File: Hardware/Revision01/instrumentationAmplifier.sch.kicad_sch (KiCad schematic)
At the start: 10 parts, among them J11 Conn_01x04, U4 TLV9062IDSGR

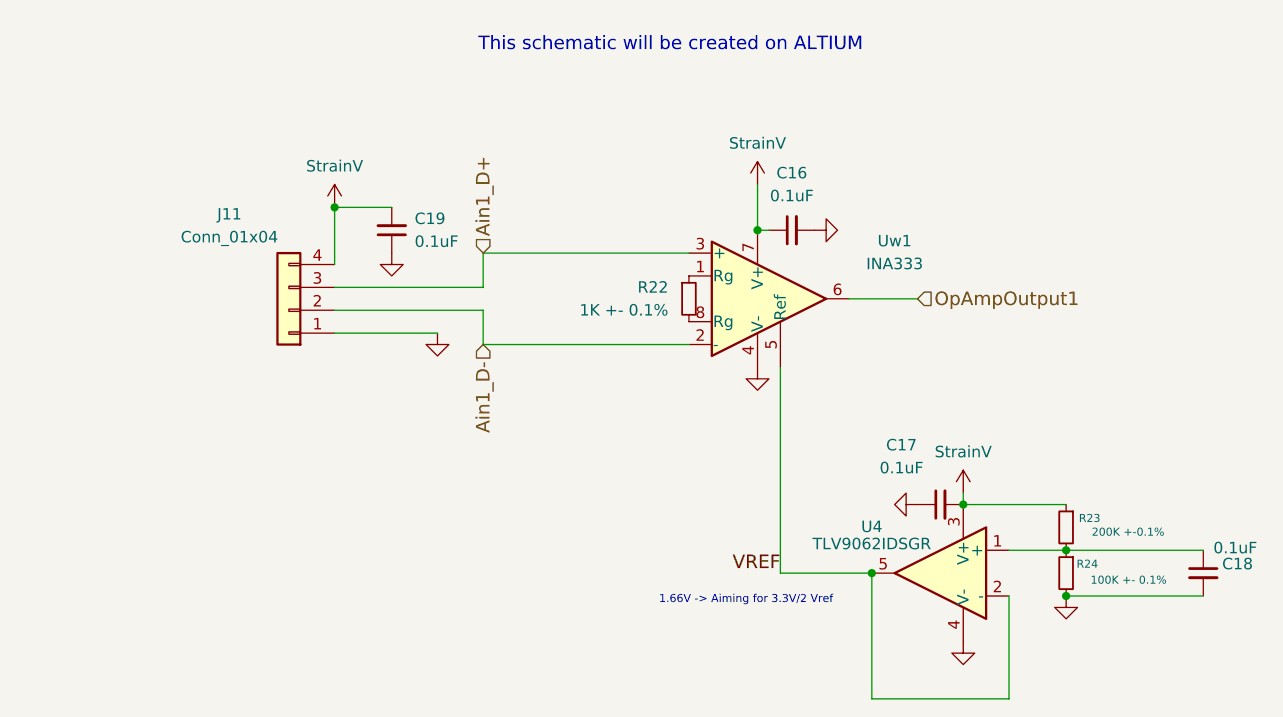
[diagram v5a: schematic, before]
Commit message: Small details on PART B, restarting component placement on PART A
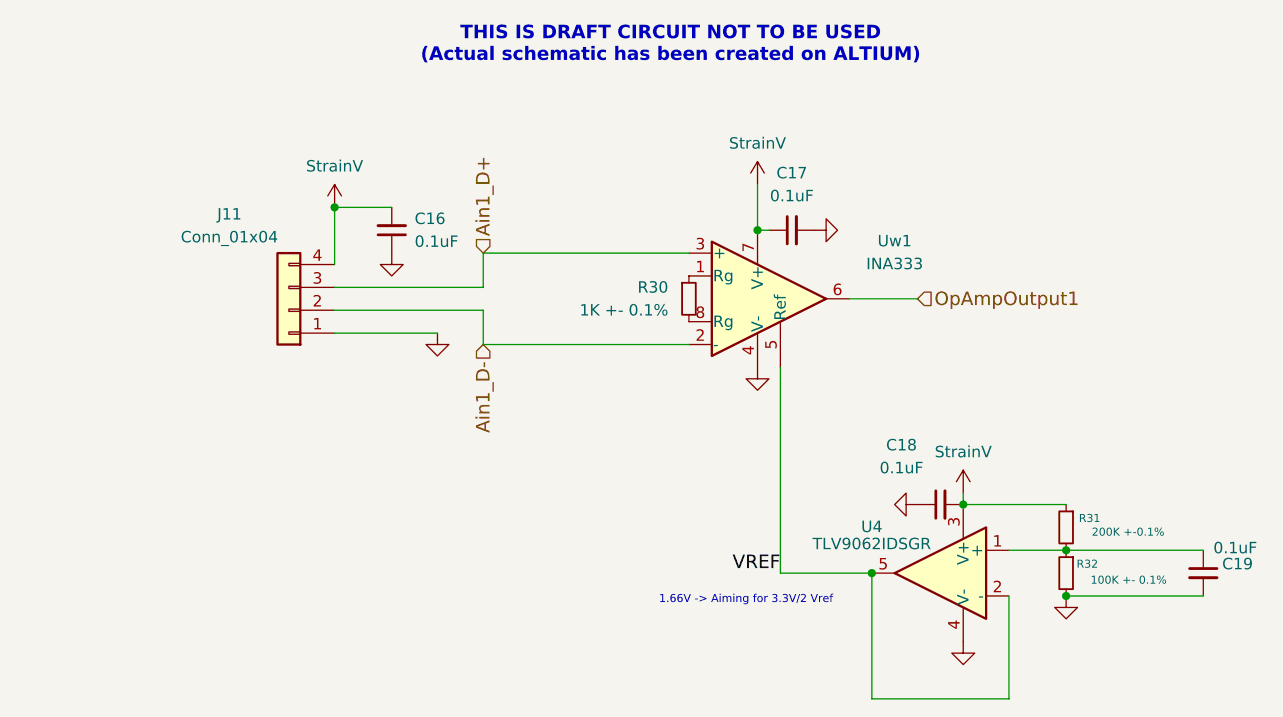
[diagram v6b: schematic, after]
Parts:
- renumbered C19 to C16, C16 to C17, C17 to C18, C18 to C19, R22 to R30, R23 to R31, R24 to R32
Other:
- note added: "THIS IS DRAFT CIRCUIT NOT TO BE USED (Actual schematic has been created on ALTIUM)"
- note removed: "This schematic will be created on ALTIUM"
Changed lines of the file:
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@@
 	(generator_version "9.0")
 	(paper "A4")
-	(text "This schematic will be created on ALTIUM"
+	(text "THIS IS DRAFT CIRCUIT NOT TO BE USED\n(Actual schematic has been created on ALTIUM)"
 		(exclude_from_sim no)
 		(at 127.508 56.896 0)
@@
 			(font
 				(size 1.4986 1.4986)
+				(thickness 0.2997)
+				(bold yes)
 			)
 		)
@@
 		(on_board no)
 		(dnp no)
-		(property "Reference" "#PWR060"
+		(property "Reference" "#PWR063"
 			(at 137.16 76.2 0)
 			(effects
@@
 			(project "Revision01"
 				(path "/955cc99e-a129-42cf-abc7-aa99813fdb5f/00000000-0000-0000-0000-00005eb1de63/14eb51a3-67a8-4f4f-b7c1-d030be0d073f"
-					(reference "#PWR060")
+					(reference "#PWR063")
 					(unit 1)
 				)
@@
 		(dnp no)
 		(fields_autoplaced yes)
-		(property "Reference" "C19"
+		(property "Reference" "C16"
 			(at 99.06 76.1935 0)
 			(effects
@@
 			(project "Revision01"
 				(path "/955cc99e-a129-42cf-abc7-aa99813fdb5f/00000000-0000-0000-0000-00005eb1de63/14eb51a3-67a8-4f4f-b7c1-d030be0d073f"
-					(reference "C19")
+					(reference "C16")
 					(unit 1)
 				)
@@
 		(on_board no)
 		(dnp no)
-		(property "Reference" "#PWR068"
+		(property "Reference" "#PWR060"
 			(at 90.17 78.74 0)
 			(effects
@@
 			(project "Revision01"
 				(path "/955cc99e-a129-42cf-abc7-aa99813fdb5f/00000000-0000-0000-0000-00005eb1de63/14eb51a3-67a8-4f4f-b7c1-d030be0d073f"
-					(reference "#PWR068")
+					(reference "#PWR060")
 					(unit 1)
 				)
@@
 		(on_board no)
 		(dnp no)
-		(property "Reference" "R24"
+		(property "Reference" "R32"
 			(at 175.006 114.554 0)
 			(effects
@@
 			(project "Revision01"
 				(path "/955cc99e-a129-42cf-abc7-aa99813fdb5f/00000000-0000-0000-0000-00005eb1de63/14eb51a3-67a8-4f4f-b7c1-d030be0d073f"
-					(reference "R24")
+					(reference "R32")
 					(unit 1)
 				)
@@
 		(on_board no)
 		(dnp no)
-		(property "Reference" "#PWR064"
+		(property "Reference" "#PWR067"
 			(at 160.02 110.49 0)
 			(effects
@@
 			(project "Revision01"
 				(path "/955cc99e-a129-42cf-abc7-aa99813fdb5f/00000000-0000-0000-0000-00005eb1de63/14eb51a3-67a8-4f4f-b7c1-d030be0d073f"
-					(reference "#PWR064")
+					(reference "#PWR067")
 					(unit 1)
 				)
@@
 		(on_board no)
 		(dnp no)
-		(property "Reference" "C18"
+		(property "Reference" "C19"
 			(at 190.5 114.554 0)
 			(effects
@@
 			(project "Revision01"
 				(path "/955cc99e-a129-42cf-abc7-aa99813fdb5f/00000000-0000-0000-0000-00005eb1de63/14eb51a3-67a8-4f4f-b7c1-d030be0d073f"
-					(reference "C18")
+					(reference "C19")
 					(unit 1)
 				)
@@
 		(dnp no)
 		(fields_autoplaced yes)
-		(property "Reference" "#PWR067"
+		(property "Reference" "#PWR062"
 			(at 101.6 95.25 0)
 			(effects
@@
 			(project "Revision01"
 				(path "/955cc99e-a129-42cf-abc7-aa99813fdb5f/00000000-0000-0000-0000-00005eb1de63/14eb51a3-67a8-4f4f-b7c1-d030be0d073f"
-					(reference "#PWR067")
+					(reference "#PWR062")
 					(unit 1)
 				)
@@
 		(dnp no)
 		(fields_autoplaced yes)
-		(property "Reference" "#PWR061"
+		(property "Reference" "#PWR064"
 			(at 137.16 99.06 0)
 			(effects
@@
 			(project "Revision01"
 				(path "/955cc99e-a129-42cf-abc7-aa99813fdb5f/00000000-0000-0000-0000-00005eb1de63/14eb51a3-67a8-4f4f-b7c1-d030be0d073f"
-					(reference "#PWR061")
+					(reference "#PWR064")
 					(unit 1)
 				)
@@
 		(dnp no)
 		(fields_autoplaced yes)
-		(property "Reference" "C16"
+		(property "Reference" "C17"
 			(at 140.9763 71.12 90)
 			(effects
@@
 			(project "Revision01"
 				(path "/955cc99e-a129-42cf-abc7-aa99813fdb5f/00000000-0000-0000-0000-00005eb1de63/14eb51a3-67a8-4f4f-b7c1-d030be0d073f"
-					(reference "C16")
+					(reference "C17")
 					(unit 1)
 				)
@@
 		(on_board no)
 		(dnp no)
-		(property "Reference" "C17"
+		(property "Reference" "C18"
 			(at 153.162 101.346 90)
 			(effects
@@
 			(project "Revision01"
 				(path "/955cc99e-a129-42cf-abc7-aa99813fdb5f/00000000-0000-0000-0000-00005eb1de63/14eb51a3-67a8-4f4f-b7c1-d030be0d073f"
-					(reference "C17")
+					(reference "C18")
 					(unit 1)
 				)
@@
 		(on_board no)
 		(dnp no)
-		(property "Reference" "R22"
+		(property "Reference" "R30"
 			(at 127.254 83.82 0)
 			(effects
@@
 			(project "Revision01"
 				(path "/955cc99e-a129-42cf-abc7-aa99813fdb5f/00000000-0000-0000-0000-00005eb1de63/14eb51a3-67a8-4f4f-b7c1-d030be0d073f"
-					(reference "R22")
+					(reference "R30")
 					(unit 1)
 				)
@@
 		(dnp no)
 		(fields_autoplaced yes)
-		(property "Reference" "#PWR065"
+		(property "Reference" "#PWR068"
 			(at 160.02 129.54 0)
 			(effects
@@
 			(project "Revision01"
 				(path "/955cc99e-a129-42cf-abc7-aa99813fdb5f/00000000-0000-0000-0000-00005eb1de63/14eb51a3-67a8-4f4f-b7c1-d030be0d073f"
-					(reference "#PWR065")
+					(reference "#PWR068")
 					(unit 1)
 				)
@@
 		(dnp no)
 		(fields_autoplaced yes)
-		(property "Reference" "#PWR062"
+		(property "Reference" "#PWR065"
 			(at 149.86 77.47 0)
 			(effects
@@
 			(project "Revision01"
 				(path "/955cc99e-a129-42cf-abc7-aa99813fdb5f/00000000-0000-0000-0000-00005eb1de63/14eb51a3-67a8-4f4f-b7c1-d030be0d073f"
-					(reference "#PWR062")
+					(reference "#PWR065")
 					(unit 1)
 				)
@@
 		(on_board no)
 		(dnp no)
-		(property "Reference" "R23"
+		(property "Reference" "R31"
 			(at 175.26 109.474 0)
 			(effects
@@
 			(project "Revision01"
 				(path "/955cc99e-a129-42cf-abc7-aa99813fdb5f/00000000-0000-0000-0000-00005eb1de63/14eb51a3-67a8-4f4f-b7c1-d030be0d073f"
-					(reference "R23")
+					(reference "R31")
 					(unit 1)
 				)
@@
 		(dnp no)
 		(fields_autoplaced yes)
-		(property "Reference" "#PWR069"
+		(property "Reference" "#PWR061"
 			(at 96.52 86.36 0)
 			(effects
@@
 			(project "Revision01"
 				(path "/955cc99e-a129-42cf-abc7-aa99813fdb5f/00000000-0000-0000-0000-00005eb1de63/14eb51a3-67a8-4f4f-b7c1-d030be0d073f"
-					(reference "#PWR069")
+					(reference "#PWR061")
 					(unit 1)
 				)
@@
 		(dnp no)
 		(fields_autoplaced yes)
-		(property "Reference" "#PWR066"
+		(property "Reference" "#PWR069"
 			(at 171.45 124.46 0)
 			(effects
@@
 			(project "Revision01"
 				(path "/955cc99e-a129-42cf-abc7-aa99813fdb5f/00000000-0000-0000-0000-00005eb1de63/14eb51a3-67a8-4f4f-b7c1-d030be0d073f"
-					(reference "#PWR066")
+					(reference "#PWR069")
 					(unit 1)
 				)
@@
 		(dnp no)
 		(fields_autoplaced yes)
-		(property "Reference" "#PWR063"
+		(property "Reference" "#PWR066"
 			(at 148.59 107.95 0)
 			(effects
@@
 			(project "Revision01"
 				(path "/955cc99e-a129-42cf-abc7-aa99813fdb5f/00000000-0000-0000-0000-00005eb1de63/14eb51a3-67a8-4f4f-b7c1-d030be0d073f"
-					(reference "#PWR063")
+					(reference "#PWR066")
 					(unit 1)
 				)

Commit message: COMPONENT LAYOUT COMPLETE
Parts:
- renumbered J11 to J13
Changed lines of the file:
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@@
 		(on_board no)
 		(dnp no)
-		(property "Reference" "#PWR063"
+		(property "Reference" "#PWR062"
 			(at 137.16 76.2 0)
 			(effects
@@
 			(project "Revision01"
 				(path "/955cc99e-a129-42cf-abc7-aa99813fdb5f/00000000-0000-0000-0000-00005eb1de63/14eb51a3-67a8-4f4f-b7c1-d030be0d073f"
-					(reference "#PWR063")
+					(reference "#PWR062")
 					(unit 1)
 				)
@@
 		(on_board yes)
 		(dnp no)
-		(property "Reference" "J11"
+		(property "Reference" "J13"
 			(at 78.486 75.692 0)
 			(effects
@@
 			(project ""
 				(path "/955cc99e-a129-42cf-abc7-aa99813fdb5f/00000000-0000-0000-0000-00005eb1de63/14eb51a3-67a8-4f4f-b7c1-d030be0d073f"
-					(reference "J11")
+					(reference "J13")
 					(unit 1)
 				)
@@
 		(on_board no)
 		(dnp no)
-		(property "Reference" "#PWR060"
+		(property "Reference" "#PWR059"
 			(at 90.17 78.74 0)
 			(effects
@@
 			(project "Revision01"
 				(path "/955cc99e-a129-42cf-abc7-aa99813fdb5f/00000000-0000-0000-0000-00005eb1de63/14eb51a3-67a8-4f4f-b7c1-d030be0d073f"
-					(reference "#PWR060")
+					(reference "#PWR059")
 					(unit 1)
 				)
@@
 		(on_board no)
 		(dnp no)
-		(property "Reference" "#PWR067"
+		(property "Reference" "#PWR066"
 			(at 160.02 110.49 0)
 			(effects
@@
 			(project "Revision01"
 				(path "/955cc99e-a129-42cf-abc7-aa99813fdb5f/00000000-0000-0000-0000-00005eb1de63/14eb51a3-67a8-4f4f-b7c1-d030be0d073f"
-					(reference "#PWR067")
+					(reference "#PWR066")
 					(unit 1)
 				)
@@
 		(dnp no)
 		(fields_autoplaced yes)
-		(property "Reference" "#PWR062"
+		(property "Reference" "#PWR061"
 			(at 101.6 95.25 0)
 			(effects
@@
 			(project "Revision01"
 				(path "/955cc99e-a129-42cf-abc7-aa99813fdb5f/00000000-0000-0000-0000-00005eb1de63/14eb51a3-67a8-4f4f-b7c1-d030be0d073f"
-					(reference "#PWR062")
+					(reference "#PWR061")
 					(unit 1)
 				)
@@
 		(dnp no)
 		(fields_autoplaced yes)
-		(property "Reference" "#PWR064"
+		(property "Reference" "#PWR063"
 			(at 137.16 99.06 0)
 			(effects
@@
 			(project "Revision01"
 				(path "/955cc99e-a129-42cf-abc7-aa99813fdb5f/00000000-0000-0000-0000-00005eb1de63/14eb51a3-67a8-4f4f-b7c1-d030be0d073f"
-					(reference "#PWR064")
+					(reference "#PWR063")
 					(unit 1)
 				)
@@
 		(dnp no)
 		(fields_autoplaced yes)
-		(property "Reference" "#PWR068"
+		(property "Reference" "#PWR067"
 			(at 160.02 129.54 0)
 			(effects
@@
 			(project "Revision01"
 				(path "/955cc99e-a129-42cf-abc7-aa99813fdb5f/00000000-0000-0000-0000-00005eb1de63/14eb51a3-67a8-4f4f-b7c1-d030be0d073f"
-					(reference "#PWR068")
+					(reference "#PWR067")
 					(unit 1)
 				)
@@
 		(dnp no)
 		(fields_autoplaced yes)
-		(property "Reference" "#PWR065"
+		(property "Reference" "#PWR064"
 			(at 149.86 77.47 0)
 			(effects
@@
 			(project "Revision01"
 				(path "/955cc99e-a129-42cf-abc7-aa99813fdb5f/00000000-0000-0000-0000-00005eb1de63/14eb51a3-67a8-4f4f-b7c1-d030be0d073f"
-					(reference "#PWR065")
+					(reference "#PWR064")
 					(unit 1)
 				)
@@
 		(dnp no)
 		(fields_autoplaced yes)
-		(property "Reference" "#PWR061"
+		(property "Reference" "#PWR060"
 			(at 96.52 86.36 0)
 			(effects
@@
 			(project "Revision01"
 				(path "/955cc99e-a129-42cf-abc7-aa99813fdb5f/00000000-0000-0000-0000-00005eb1de63/14eb51a3-67a8-4f4f-b7c1-d030be0d073f"
-					(reference "#PWR061")
+					(reference "#PWR060")
 					(unit 1)
 				)
@@
 		(dnp no)
 		(fields_autoplaced yes)
-		(property "Reference" "#PWR069"
+		(property "Reference" "#PWR068"
 			(at 171.45 124.46 0)
 			(effects
@@
 			(project "Revision01"
 				(path "/955cc99e-a129-42cf-abc7-aa99813fdb5f/00000000-0000-0000-0000-00005eb1de63/14eb51a3-67a8-4f4f-b7c1-d030be0d073f"
-					(reference "#PWR069")
+					(reference "#PWR068")
 					(unit 1)
 				)
@@
 		(dnp no)
 		(fields_autoplaced yes)
-		(property "Reference" "#PWR066"
+		(property "Reference" "#PWR065"
 			(at 148.59 107.95 0)
 			(effects
@@
 			(project "Revision01"
 				(path "/955cc99e-a129-42cf-abc7-aa99813fdb5f/00000000-0000-0000-0000-00005eb1de63/14eb51a3-67a8-4f4f-b7c1-d030be0d073f"
-					(reference "#PWR066")
+					(reference "#PWR065")
 					(unit 1)
 				)

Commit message: PART A schematic - debugging headers added, DRC has been checked, initial gerberfiles created(not checked)
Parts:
- C16, C17, C18, C19, J13, R30, R31, R32, U4, Uw1: now left out of the parts list
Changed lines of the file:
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@@
 		(unit 1)
 		(exclude_from_sim no)
-		(in_bom yes)
+		(in_bom no)
 		(on_board no)
 		(dnp no)
@@
 		(unit 1)
 		(exclude_from_sim no)
-		(in_bom yes)
+		(in_bom no)
 		(on_board yes)
 		(dnp no)
@@
 		)
 		(property "Description" "Generic connector, single row, 01x04, script generated (kicad-library-utils/schlib/autogen/connector/)"
+			(at 85.09 86.36 0)
+			(effects
+				(font
+					(size 1.27 1.27)
+				)
+				(hide yes)
+			)
+		)
+		(property "Sim.Type" ""
 			(at 85.09 86.36 0)
 			(effects
@@
 		(unit 1)
 		(exclude_from_sim no)
-		(in_bom yes)
+		(in_bom no)
 		(on_board no)
 		(dnp no)
@@
 					(size 1.27 1.27)
 				)
+			)
+		)
+		(property "Sim.Type" ""
+			(at 96.52 77.47 0)
+			(effects
+				(font
+					(size 1.27 1.27)
+				)
+				(hide yes)
 			)
 		)
@@
 		(unit 1)
 		(exclude_from_sim no)
-		(in_bom yes)
+		(in_bom no)
 		(on_board no)
 		(dnp no)
@@
 		(unit 1)
 		(exclude_from_sim no)
-		(in_bom yes)
+		(in_bom no)
 		(on_board no)
 		(dnp no)
@@
 					(size 1.27 1.27)
 				)
+			)
+		)
+		(property "Sim.Type" ""
+			(at 171.45 115.57 0)
+			(effects
+				(font
+					(size 1.27 1.27)
+				)
+				(hide yes)
 			)
 		)
@@
 		(unit 1)
 		(exclude_from_sim no)
-		(in_bom yes)
+		(in_bom no)
 		(on_board no)
 		(dnp no)
@@
 		(unit 1)
 		(exclude_from_sim no)
-		(in_bom yes)
+		(in_bom no)
 		(on_board no)
 		(dnp no)
@@
 					(size 1.27 1.27)
 				)
+			)
+		)
+		(property "Sim.Type" ""
+			(at 186.69 115.57 0)
+			(effects
+				(font
+					(size 1.27 1.27)
+				)
+				(hide yes)
 			)
 		)
@@
 		(unit 1)
 		(exclude_from_sim no)
-		(in_bom yes)
+		(in_bom no)
 		(on_board no)
 		(dnp no)
@@
 		(unit 1)
 		(exclude_from_sim no)
-		(in_bom yes)
+		(in_bom no)
 		(on_board no)
 		(dnp no)
@@
 		(unit 1)
 		(exclude_from_sim no)
-		(in_bom yes)
+		(in_bom no)
 		(on_board no)
 		(dnp no)
@@
 					(size 1.27 1.27)
 				)
+			)
+		)
+		(property "Sim.Type" ""
+			(at 140.97 77.47 90)
+			(effects
+				(font
+					(size 1.27 1.27)
+				)
+				(hide yes)
 			)
 		)
@@
 		(unit 1)
 		(exclude_from_sim no)
-		(in_bom yes)
+		(in_bom no)
 		(on_board no)
 		(dnp no)
@@
 					(size 1.27 1.27)
 				)
+			)
+		)
+		(property "Sim.Type" ""
+			(at 157.48 107.95 90)
+			(effects
+				(font
+					(size 1.27 1.27)
+				)
+				(hide yes)
 			)
 		)
@@
 		(unit 1)
 		(exclude_from_sim no)
-		(in_bom yes)
+		(in_bom no)
 		(on_board no)
 		(dnp no)
@@
 					(size 1.27 1.27)
 				)
+			)
+		)
+		(property "Sim.Type" ""
+			(at 129.54 85.09 0)
+			(effects
+				(font
+					(size 1.27 1.27)
+				)
+				(hide yes)
 			)
 		)
@@
 		(unit 1)
 		(exclude_from_sim no)
-		(in_bom yes)
+		(in_bom no)
 		(on_board no)
 		(dnp no)
@@
 					(size 1.27 1.27)
 				)
+			)
+		)
+		(property "Sim.Type" ""
+			(at 157.48 115.57 0)
+			(effects
+				(font
+					(size 1.27 1.27)
+				)
+				(hide yes)
 			)
 		)
@@
 		(unit 1)
 		(exclude_from_sim no)
-		(in_bom yes)
+		(in_bom no)
 		(on_board no)
 		(dnp no)
@@
 		(unit 1)
 		(exclude_from_sim no)
-		(in_bom yes)
+		(in_bom no)
 		(on_board no)
 		(dnp no)
@@
 		(unit 1)
 		(exclude_from_sim no)
-		(in_bom yes)
+		(in_bom no)
 		(on_board no)
 		(dnp no)
@@
 					(size 1.27 1.27)
 				)
+			)
+		)
+		(property "Sim.Type" ""
+			(at 137.16 85.09 0)
+			(effects
+				(font
+					(size 1.27 1.27)
+				)
+				(hide yes)
 			)
 		)
@@
 		(unit 1)
 		(exclude_from_sim no)
-		(in_bom yes)
+		(in_bom no)
 		(on_board no)
 		(dnp no)
@@
 					(size 1.27 1.27)
 				)
+			)
+		)
+		(property "Sim.Type" ""
+			(at 171.45 110.49 0)
+			(effects
+				(font
+					(size 1.27 1.27)
+				)
+				(hide yes)
 			)
 		)
@@
 		(unit 1)
 		(exclude_from_sim no)
-		(in_bom yes)
+		(in_bom no)
 		(on_board no)
 		(dnp no)
@@
 		(unit 1)
 		(exclude_from_sim no)
-		(in_bom yes)
+		(in_bom no)
 		(on_board no)
 		(dnp no)
@@
 		(unit 1)
 		(exclude_from_sim no)
-		(in_bom yes)
+		(in_bom no)
 		(on_board no)
 		(dnp no)
